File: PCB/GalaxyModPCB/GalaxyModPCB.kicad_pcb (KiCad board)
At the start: 2 copper layers, 63.5 x 38.2 mm, 57 parts, among them J1 LED RGBW Connector, J2 USB to UART, J3 Motor Connector, J4 Projector Connector, J6 Power Header, J7 Boot mode, Q1 IRLML0030, Q2 IRLML0030, Q3 IRLML0030, Q4 IRLML0030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

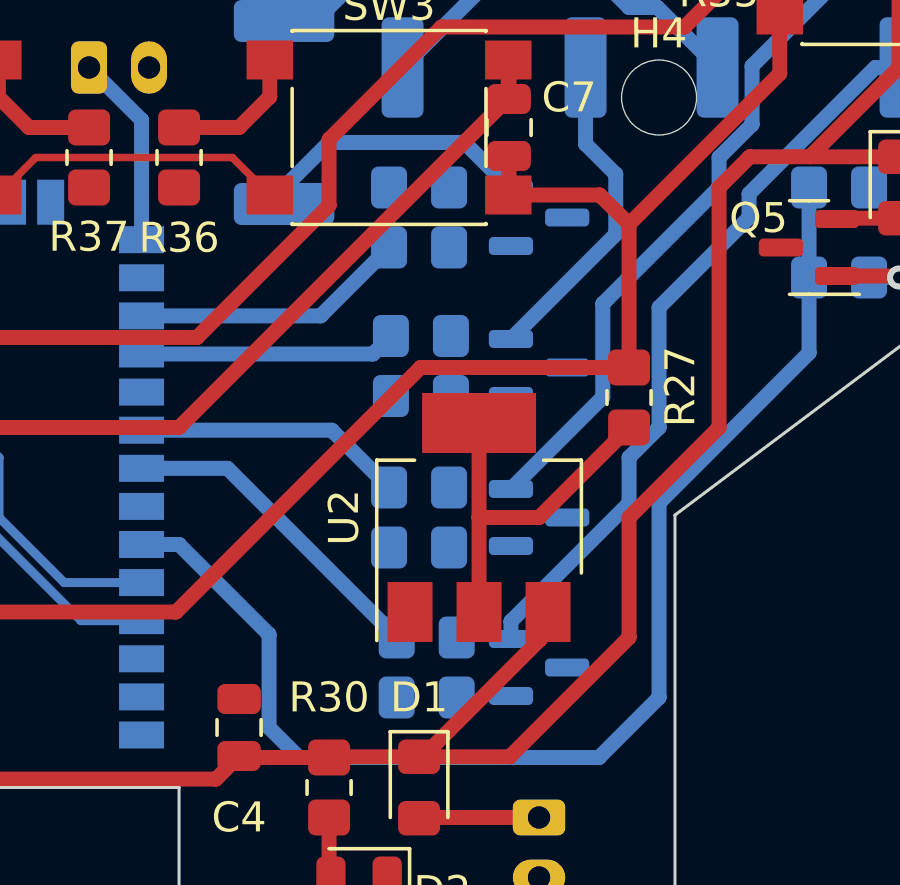
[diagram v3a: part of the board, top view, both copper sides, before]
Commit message: Connected transistors
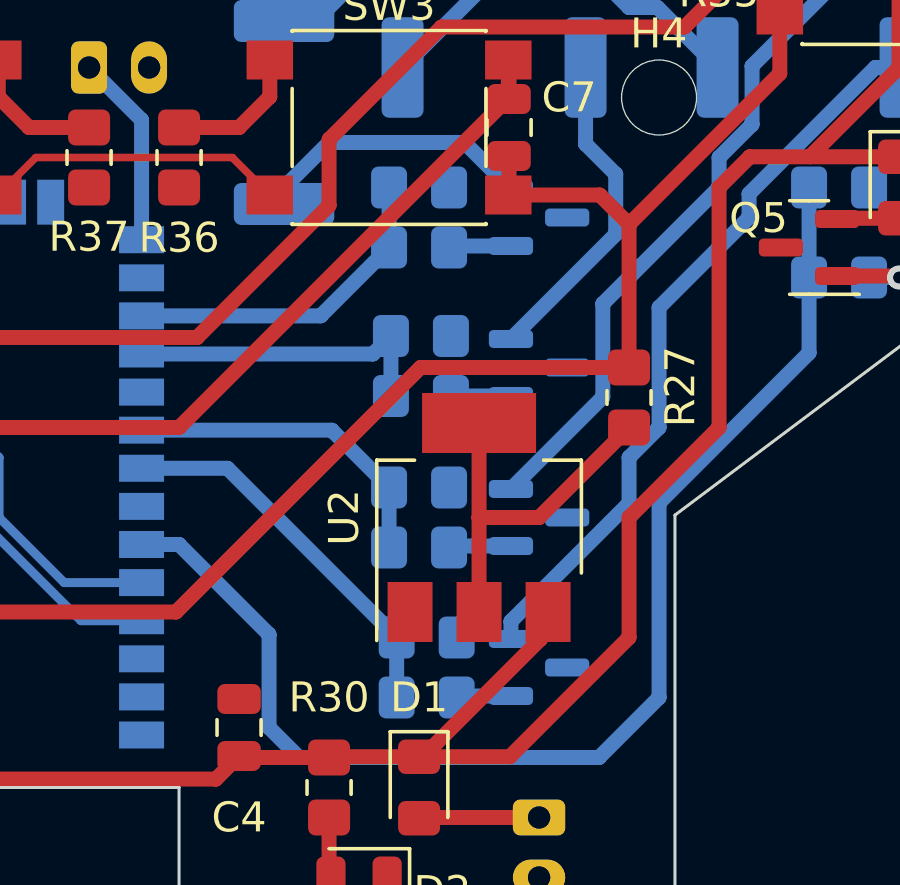
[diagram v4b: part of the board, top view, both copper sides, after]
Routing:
- net Net-(Q3-Pad1): track 0.00 -> 2.08 mm
- net Net-(Q1-Pad1): track 0.00 -> 2.08 mm
- net Net-(R20-Pad1): track 10.8 -> 12.8 mm
- net Net-(R19-Pad1): track 9.04 -> 11.0 mm
- net Net-(R18-Pad1): track 8.56 -> 10.6 mm
- net Net-(R17-Pad1): track 9.19 -> 11.2 mm
- net Net-(Q2-Pad1): track 0.00 -> 2.00 mm
- net Net-(Q4-Pad1): track 0.00 -> 1.83 mm
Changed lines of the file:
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@@
   (segment (start 131.5 70.5) (end 134.5 70.5) (width 0.3) (layer "B.Cu") (net 14))
   (segment (start 113 67) (end 113 65) (width 0.5) (layer "F.Cu") (net 15))
+  (segment (start 152.05 64.95) (end 152 65) (width 0.5) (layer "B.Cu") (net 16))
+  (segment (start 154.0625 64.95) (end 152.05 64.95) (width 0.5) (layer "B.Cu") (net 16))
   (segment (start 146.5 63.55) (end 146.5 63) (width 0.5) (layer "B.Cu") (net 17))
   (segment (start 146.5 63) (end 148 61.5) (width 0.5) (layer "B.Cu") (net 17))
   (segment (start 152.5125 61.5) (end 154.0625 63.05) (width 0.5) (layer "B.Cu") (net 17))
   (segment (start 148 61.5) (end 152.5125 61.5) (width 0.5) (layer "B.Cu") (net 17))
+  (segment (start 154.0625 69.95) (end 152.0625 69.95) (width 0.5) (layer "B.Cu") (net 18))
   (segment (start 156.55 61.55) (end 156.55 59) (width 0.5) (layer "B.Cu") (net 19))
   (segment (start 154.0625 68.05) (end 157.55625 64.55625) (width 0.5) (layer "B.Cu") (net 19))
   (segment (start 157.55625 62.55625) (end 157.55625 64.55625) (width 0.5) (layer "B.Cu") (net 19))
   (segment (start 156.55 61.55) (end 157.55625 62.55625) (width 0.5) (layer "B.Cu") (net 19))
+  (segment (start 154.0625 74.95) (end 152.05 74.95) (width 0.5) (layer "B.Cu") (net 20))
+  (segment (start 152.05 74.95) (end 152 75) (width 0.5) (layer "B.Cu") (net 20))
   (segment (start 157.125 66.875) (end 157.125 69.9875) (width 0.5) (layer "B.Cu") (net 21))
   (segment (start 162.1 60.9) (end 161 62) (width 0.5) (layer "B.Cu") (net 21))
@@
   (segment (start 161 62) (end 161 63) (width 0.5) (layer "B.Cu") (net 21))
   (segment (start 157.125 69.9875) (end 154.0625 73.05) (width 0.5) (layer "B.Cu") (net 21))
+  (segment (start 154.0625 79.95) (end 152.303928 79.95) (width 0.5) (layer "B.Cu") (net 22))
+  (segment (start 152.303928 79.95) (end 152.253928 80) (width 0.5) (layer "B.Cu") (net 22))
   (segment (start 158 72) (end 158 73.523528) (width 0.5) (layer "B.Cu") (net 23))
   (segment (start 166.210051 59) (end 162 63.210051) (width 0.5) (layer "B.Cu") (net 23))
@@
   (segment (start 116.0125 63) (end 116.0625 62.95) (width 0.5) (layer "F.Cu") (net 50))
   (segment (start 113 63) (end 116.0125 63) (width 0.5) (layer "F.Cu") (net 50))
+  (segment (start 150 63) (end 150 65) (width 0.5) (layer "B.Cu") (net 51))
   (segment (start 147.72 67.28) (end 150 65) (width 0.5) (layer "B.Cu") (net 51))
   (segment (start 141.75 67.28) (end 147.72 67.28) (width 0.5) (layer "B.Cu") (net 51))
+  (segment (start 150.0625 69.95) (end 150.0625 67.95) (width 0.5) (layer "B.Cu") (net 52))
   (segment (start 141.75 68.55) (end 149.4625 68.55) (width 0.5) (layer "B.Cu") (net 52))
   (segment (start 149.4625 68.55) (end 150.0625 67.95) (width 0.5) (layer "B.Cu") (net 52))
   (segment (start 150 73) (end 148.09 71.09) (width 0.5) (layer "B.Cu") (net 53))
   (segment (start 148.09 71.09) (end 141.75 71.09) (width 0.5) (layer "B.Cu") (net 53))
+  (segment (start 150 73) (end 150 75) (width 0.5) (layer "B.Cu") (net 53))
   (segment (start 144.613928 72.36) (end 150.253928 78) (width 0.5) (layer "B.Cu") (net 54))
   (segment (start 141.75 72.36) (end 144.613928 72.36) (width 0.5) (layer "B.Cu") (net 54))
+  (segment (start 150.253928 78) (end 150.253928 80) (width 0.5) (layer "B.Cu") (net 54))
   (segment (start 121 66) (end 121 68) (width 0.5) (layer "B.Cu") (net 55))
   (segment (start 122.82 69.82) (end 124.25 69.82) (width 0.5) (layer "B.Cu") (net 55))

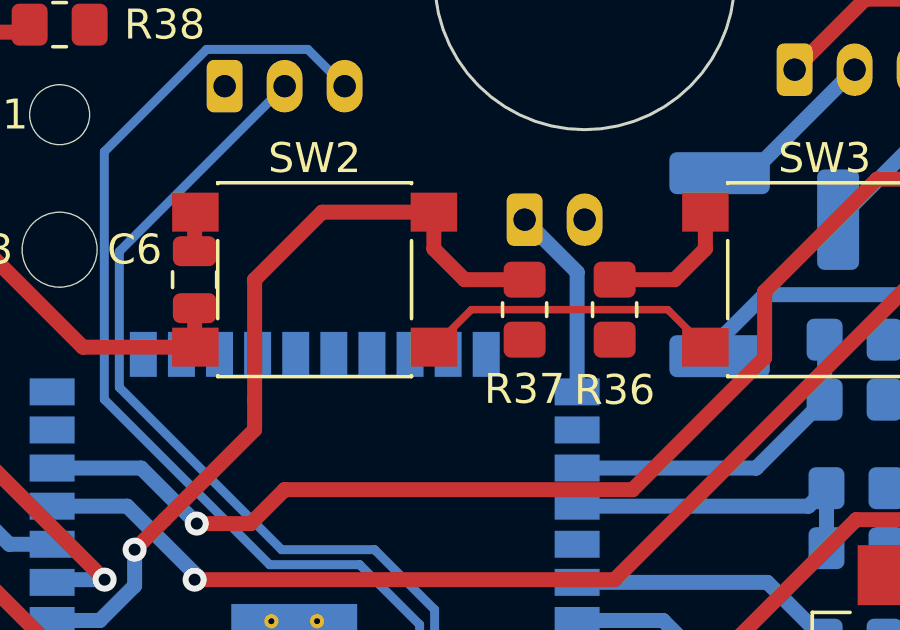
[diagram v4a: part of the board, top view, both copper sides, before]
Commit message: Neatened tracks
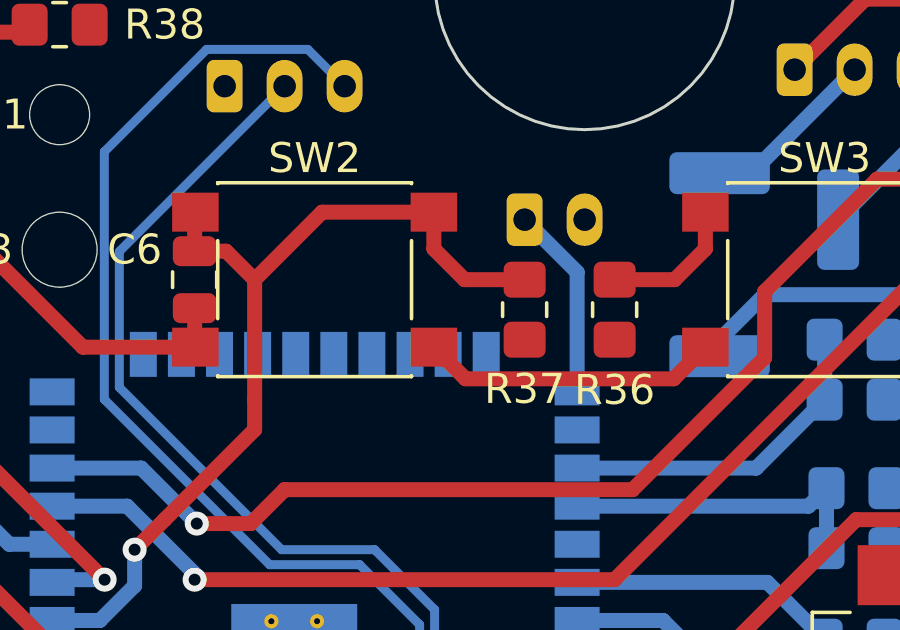
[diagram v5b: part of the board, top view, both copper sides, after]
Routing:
- net Net-(C6-Pad1): track 28.0 -> 30.4 mm
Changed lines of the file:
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@@
   (segment (start 128 69) (end 127 70) (width 0.5) (layer "F.Cu") (net 4))
   (segment (start 131 66) (end 128 69) (width 0.5) (layer "F.Cu") (net 4))
+  (segment (start 129 60.05) (end 130.05 60.05) (width 0.5) (layer "F.Cu") (net 4))
   (segment (start 136.975 58.75) (end 133.25 58.75) (width 0.5) (layer "F.Cu") (net 4))
   (segment (start 131 61) (end 131 65) (width 0.5) (layer "F.Cu") (net 4))
   (segment (start 136.975 59.975) (end 138 61) (width 0.5) (layer "F.Cu") (net 4))
   (segment (start 136.975 58.75) (end 136.975 59.975) (width 0.5) (layer "F.Cu") (net 4))
+  (segment (start 130.05 60.05) (end 131 61) (width 0.5) (layer "F.Cu") (net 4))
   (segment (start 129 58.775) (end 129.025 58.75) (width 0.5) (layer "F.Cu") (net 4))
   (segment (start 133.25 58.75) (end 131 61) (width 0.5) (layer "F.Cu") (net 4))
@@
   (segment (start 154 61.95) (end 154 63.225) (width 0.5) (layer "F.Cu") (net 7))
   (segment (start 126.05 79.185051) (end 126.05 81) (width 0.5) (layer "F.Cu") (net 7))
-  (segment (start 136.975 63.25) (end 138.225 62) (width 0.25) (layer "F.Cu") (net 7))
   (segment (start 157.025 63.25) (end 153.975 63.25) (width 0.5) (layer "F.Cu") (net 7))
   (segment (start 113 55.95) (end 113 57.225) (width 0.5) (layer "F.Cu") (net 7))
@@
   (segment (start 128 76) (end 128 77.064949) (width 0.5) (layer "F.Cu") (net 7))
   (segment (start 129 61.95) (end 129 63.225) (width 0.5) (layer "F.Cu") (net 7))
+  (segment (start 144.969975 64.305025) (end 146.025 63.25) (width 0.5) (layer "F.Cu") (net 7))
   (segment (start 125.275124 63.25) (end 120.975 58.949876) (width 0.5) (layer "F.Cu") (net 7))
-  (segment (start 138.225 62) (end 144.775 62) (width 0.25) (layer "F.Cu") (net 7))
   (segment (start 129.025 63.25) (end 125.275124 63.25) (width 0.5) (layer "F.Cu") (net 7))
-  (segment (start 144.775 62) (end 146.025 63.25) (width 0.25) (layer "F.Cu") (net 7))
+  (segment (start 136.975 63.25) (end 138.030025 64.305025) (width 0.5) (layer "F.Cu") (net 7))
   (segment (start 154 63.225) (end 153.975 63.25) (width 0.5) (layer "F.Cu") (net 7))
   (segment (start 126.05 79.95) (end 126.05 81) (width 0.5) (layer "F.Cu") (net 7))
+  (segment (start 138.030025 64.305025) (end 144.969975 64.305025) (width 0.5) (layer "F.Cu") (net 7))
   (via (at 123 80) (size 0.8) (drill 0.4) (layers "F.Cu" "B.Cu") (net 7))
   (segment (start 123 80) (end 123.02 79.98) (width 0.5) (layer "B.Cu") (net 7))

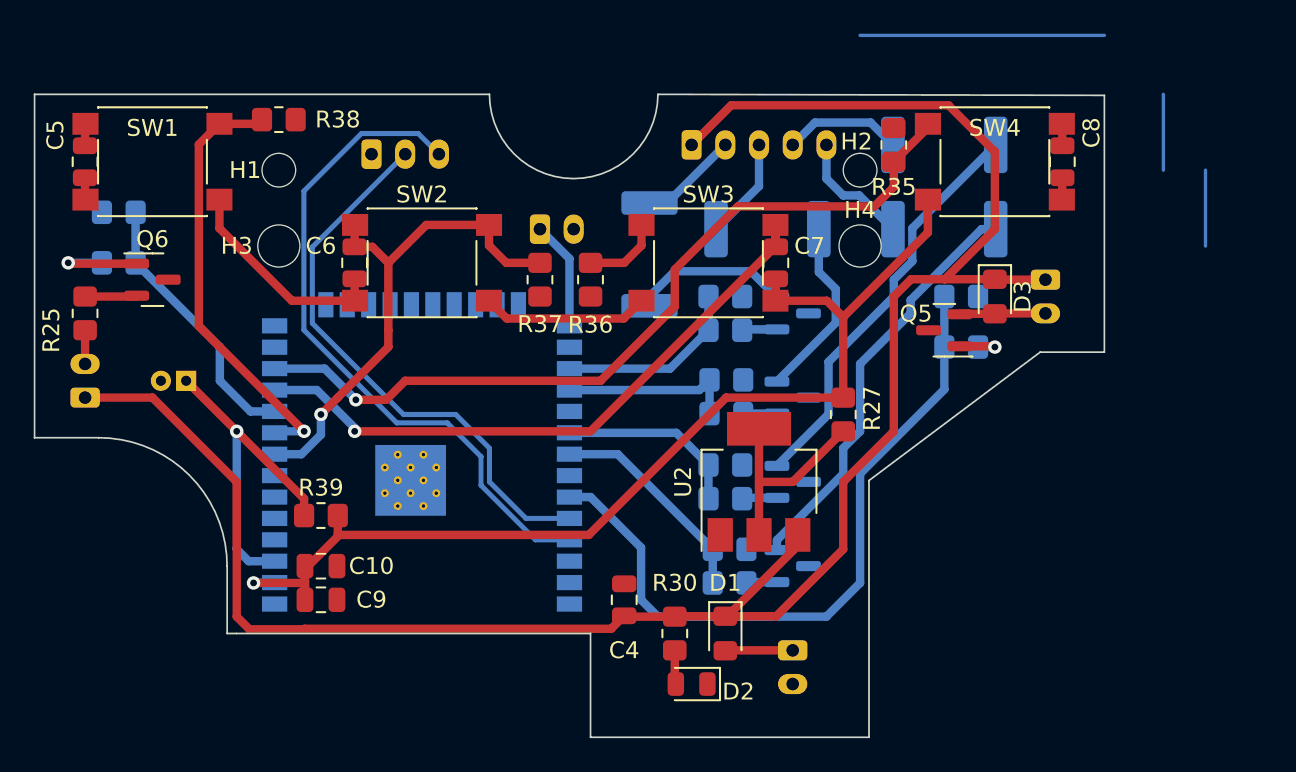
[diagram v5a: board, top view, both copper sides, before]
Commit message: Added ground fill
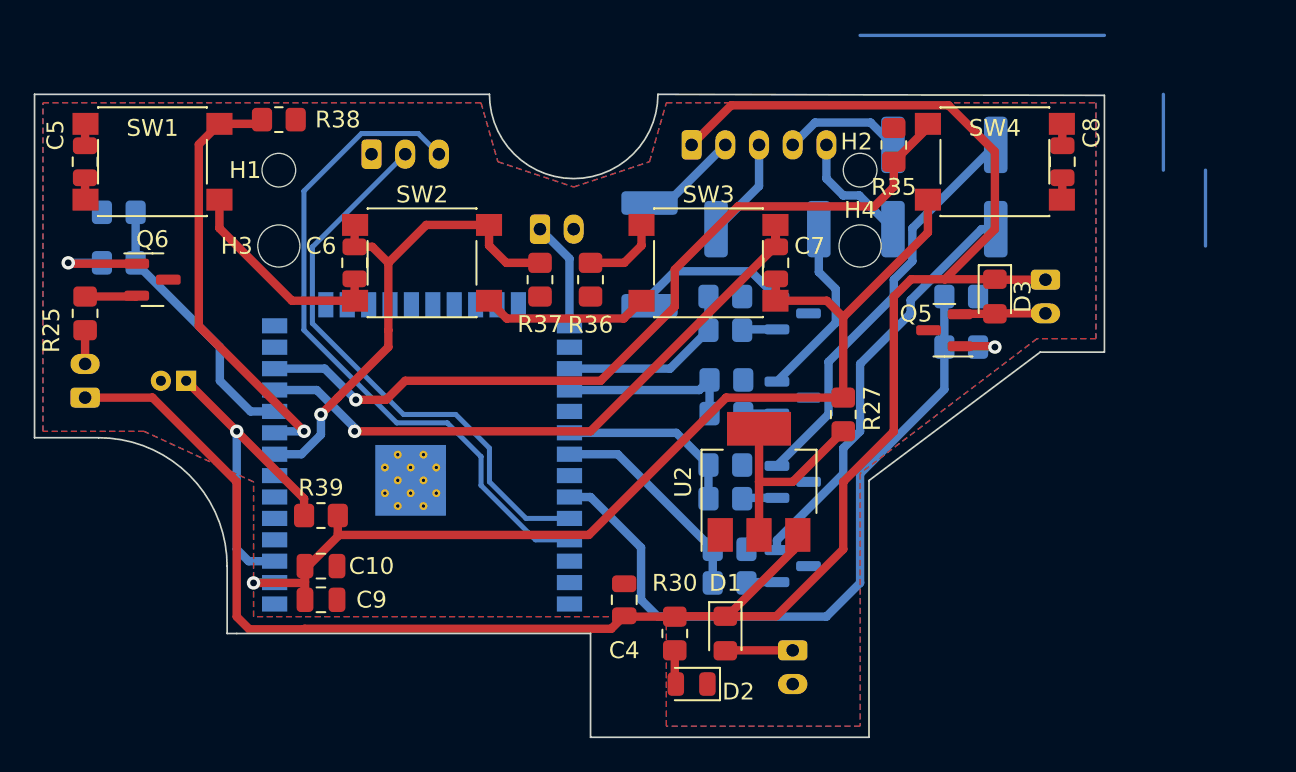
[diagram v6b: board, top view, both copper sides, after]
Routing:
- added copper zone on B.Cu, net GNDREF
- added copper zone on F.Cu, net GNDREF
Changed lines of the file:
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@@
   (segment (start 147 82) (end 157 82) (width 0.5) (layer "B.Cu") (net 56))
   (segment (start 146 81) (end 147 82) (width 0.5) (layer "B.Cu") (net 56))
+  (zone (net 2) (net_name "GNDREF") (layers F&B.Cu) (hatch edge 0.508)
+    (connect_pads (clearance 0.508))
+    (min_thickness 0.254) (filled_areas_thickness no)
+    (fill yes (thermal_gap 0.508) (thermal_bridge_width 0.508))
+    (polygon
+      (pts
+        (xy 137.5 55)
+        (xy 142 56.5)
+        (xy 146.5 55)
+        (xy 147.5 51.5)
+        (xy 173 51.5)
+        (xy 173 65.5)
+        (xy 169.5 65.5)
+        (xy 159 73.5)
+        (xy 159 88.5)
+        (xy 147.5 88.5)
+        (xy 147.5 82)
+        (xy 123 82)
+        (xy 123 74)
+        (xy 116.5 71)
+        (xy 110.5 71)
+        (xy 110.5 51.5)
+        (xy 136.5 51.5)
+      )
+    )
+  )
   (group "" (id 00b4153f-a890-4c55-b684-03c0e6cef0c4)
     (members

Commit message: Connected ground planes
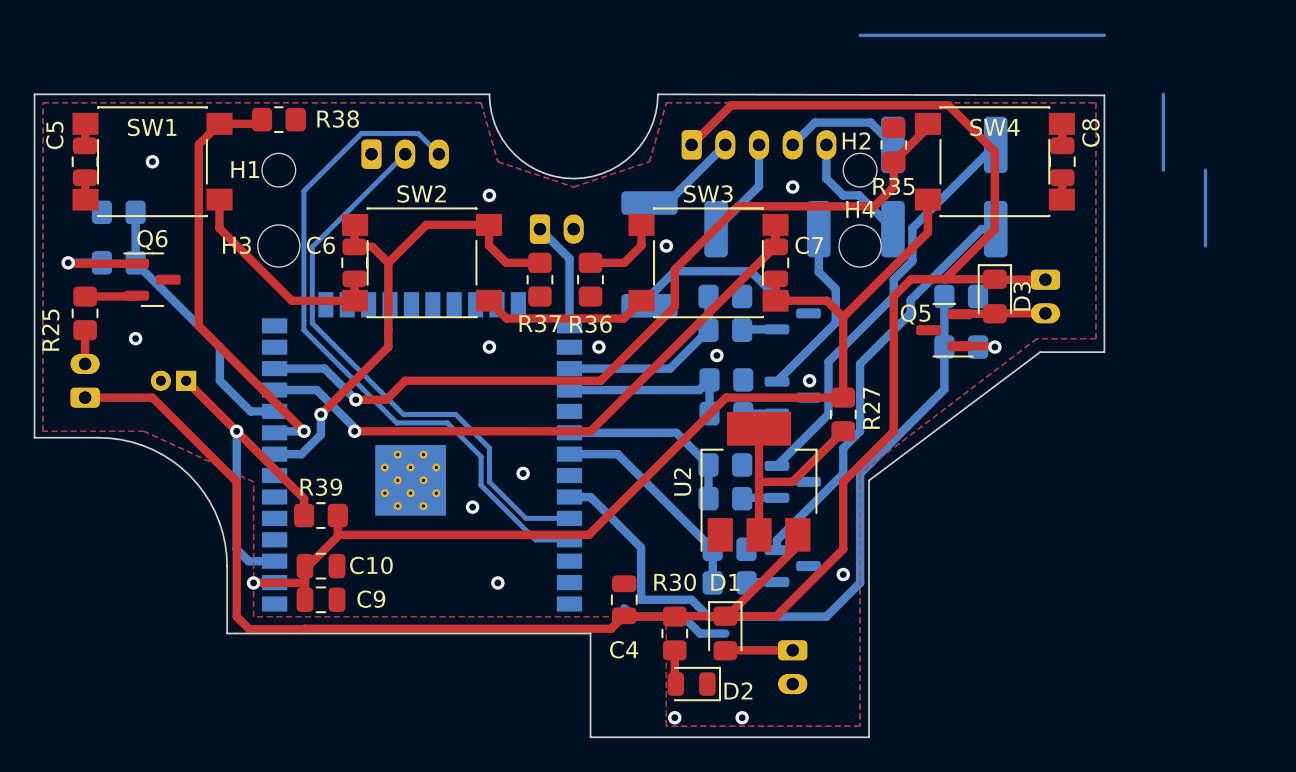
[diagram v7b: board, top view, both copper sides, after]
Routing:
- net (no net): track 0.00 -> 6.62 mm
- net GNDREF: vias 0 -> 15
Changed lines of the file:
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@@
   (gr_line (start 173.5 51.06) (end 173.5 66.3) (layer "Edge.Cuts") (width 0.1))
   (gr_line (start 113.81 71.38) (end 110 71.38) (layer "Edge.Cuts") (width 0.1))
+  (segment (start 145.5 82) (end 148.5 82) (width 0.5) (layer "B.Cu") (net 0))
+  (segment (start 145 81.5) (end 145.5 82) (width 0.5) (layer "B.Cu") (net 0))
+  (segment (start 148.5 82) (end 149.5 83) (width 0.5) (layer "B.Cu") (net 0))
+  (segment (start 149.5 83) (end 151 83) (width 0.5) (layer "B.Cu") (net 0))
   (segment (start 126 75) (end 126 76) (width 0.5) (layer "F.Cu") (net 1))
   (segment (start 122 71) (end 126 75) (width 0.5) (layer "F.Cu") (net 1))
@@
   (segment (start 122 78) (end 122.71 78.71) (width 0.5) (layer "B.Cu") (net 1))
   (segment (start 122.71 78.71) (end 124.25 78.71) (width 0.5) (layer "B.Cu") (net 1))
+  (via (at 156 68) (size 0.8) (drill 0.4) (layers "F.Cu" "B.Cu") (free) (net 2))
+  (via (at 158 79.5) (size 0.8) (drill 0.4) (layers "F.Cu" "B.Cu") (free) (net 2))
+  (via (at 148 88) (size 0.8) (drill 0.4) (layers "F.Cu" "B.Cu") (free) (net 2))
+  (via (at 137.5 80) (size 0.8) (drill 0.4) (layers "F.Cu" "B.Cu") (free) (net 2))
+  (via (at 139 73.5) (size 0.8) (drill 0.4) (layers "F.Cu" "B.Cu") (free) (net 2))
+  (via (at 136 75.5) (size 0.8) (drill 0.4) (layers "F.Cu" "B.Cu") (free) (net 2))
+  (via (at 117 55) (size 0.8) (drill 0.4) (layers "F.Cu" "B.Cu") (free) (net 2))
+  (via (at 137 57) (size 0.8) (drill 0.4) (layers "F.Cu" "B.Cu") (free) (net 2))
+  (via (at 116 65.5) (size 0.8) (drill 0.4) (layers "F.Cu" "B.Cu") (free) (net 2))
+  (via (at 143.5 66) (size 0.8) (drill 0.4) (layers "F.Cu" "B.Cu") (free) (net 2))
+  (via (at 155 56.5) (size 0.8) (drill 0.4) (layers "F.Cu" "B.Cu") (free) (net 2))
+  (via (at 150.5 66.5) (size 0.8) (drill 0.4) (layers "F.Cu" "B.Cu") (free) (net 2))
+  (via (at 137 66) (size 0.8) (drill 0.4) (layers "F.Cu" "B.Cu") (free) (net 2))
+  (via (at 147.5 60) (size 0.8) (drill 0.4) (layers "F.Cu" "B.Cu") (free) (net 2))
+  (via (at 152 88) (size 0.8) (drill 0.4) (layers "F.Cu" "B.Cu") (free) (net 2))
   (segment (start 120.975 52.75) (end 119.75 53.975) (width 0.5) (layer "F.Cu") (net 3))
   (segment (start 119.75 64.75) (end 126 71) (width 0.5) (layer "F.Cu") (net 3))
@@
   (segment (start 164 66) (end 164 63) (width 0.5) (layer "B.Cu") (net 56))
   (segment (start 159 73.513478) (end 164 68.513478) (width 0.5) (layer "B.Cu") (net 56))
+  (segment (start 146 81) (end 149 81) (width 0.5) (layer "B.Cu") (net 56))
   (segment (start 159 80) (end 159 73.513478) (width 0.5) (layer "B.Cu") (net 56))
+  (segment (start 149 81) (end 150 82) (width 0.5) (layer "B.Cu") (net 56))
   (segment (start 157 82) (end 159 80) (width 0.5) (layer "B.Cu") (net 56))
+  (segment (start 150 82) (end 157 82) (width 0.5) (layer "B.Cu") (net 56))
   (segment (start 146 77.9) (end 146 81) (width 0.5) (layer "B.Cu") (net 56))
   (segment (start 141.75 74.9) (end 143 74.9) (width 0.5) (layer "B.Cu") (net 56))
-  (segment (start 147 82) (end 157 82) (width 0.5) (layer "B.Cu") (net 56))
-  (segment (start 146 81) (end 147 82) (width 0.5) (layer "B.Cu") (net 56))
   (zone (net 2) (net_name "GNDREF") (layers F&B.Cu) (hatch edge 0.508)
     (connect_pads (clearance 0.508))
